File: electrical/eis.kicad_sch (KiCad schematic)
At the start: 26 parts

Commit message: Changed GPS 175 to not have connection to GTS 205x per g3xpert. Moved ELT GPS from GPS 175 and used RS-232 on GDU 460 for GEA 24 backup.
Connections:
- net SERIAL_IN: now reaches GEA24.P241_4 (RS-232_RX)
- net SERIAL_OUT: now reaches GEA24.P241_5 (RS-232_TX)
- net SERIAL_GND: now reaches GEA24.P241_6 (SIGNAL_GND)
- no-connect marks 20 -> 17
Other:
- note removed: "Not enough serial ports on GDU"
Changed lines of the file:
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@@
 	(title_block
 		(title "EIS")
-		(date "2025-09-08")
-		(rev "1.0")
+		(date "2025-09-09")
+		(rev "1.0.1")
 		(company "N78HR")
 	)
@@
 			)
 			(justify left)
-		)
-	)
-	(text "Not enough serial\nports on GDU"
-		(exclude_from_sim no)
-		(at 80.264 39.116 0)
-		(effects
-			(font
-				(size 1.27 1.27)
-			)
 		)
 	)
@@
 	)
 	(no_connect
-		(at 67.31 36.83)
-	)
-	(no_connect
-		(at 67.31 41.91)
-	)
-	(no_connect
 		(at 95.25 134.62)
 	)
@@
 	)
 	(no_connect
-		(at 67.31 39.37)
-	)
-	(no_connect
 		(at 67.31 220.98)
 	)
@@
 	(wire
 		(pts
+			(xy 67.31 41.91) (xy 78.74 41.91)
+		)
+		(stroke
+			(width 0)
+			(type default)
+		)
+	)
+	(wire
+		(pts
 			(xy 86.36 106.68) (xy 67.31 106.68)
 		)
@@
 	(wire
 		(pts
+			(xy 67.31 39.37) (xy 78.74 39.37)
+		)
+		(stroke
+			(width 0)
+			(type default)
+		)
+	)
+	(wire
+		(pts
 			(xy 67.31 177.8) (xy 95.25 177.8)
 		)
@@
 		(pts
 			(xy 67.31 26.67) (xy 78.74 26.67)
+		)
+		(stroke
+			(width 0)
+			(type default)
+		)
+	)
+	(wire
+		(pts
+			(xy 67.31 36.83) (xy 78.74 36.83)
 		)
 		(stroke
@@
 		)
 	)
+	(hierarchical_label "SERIAL_OUT"
+		(shape output)
+		(at 78.74 36.83 0)
+		(effects
+			(font
+				(size 1.27 1.27)
+			)
+			(justify left)
+		)
+	)
 	(hierarchical_label "GEA24_PWR"
 		(shape input)
@@
 		)
 	)
+	(hierarchical_label "SERIAL_GND"
+		(shape passive)
+		(at 78.74 41.91 0)
+		(effects
+			(font
+				(size 1.27 1.27)
+			)
+			(justify left)
+		)
+	)
 	(hierarchical_label "IGN_BAK_LOW_VOLTS"
 		(shape input)
@@
 		(effects
 			(font
+				(size 1.27 1.27)
+			)
+			(justify left)
+		)
+	)
+	(hierarchical_label "SERIAL_IN"
+		(shape input)
+		(at 78.74 39.37 0)
+		(effects
+			(font

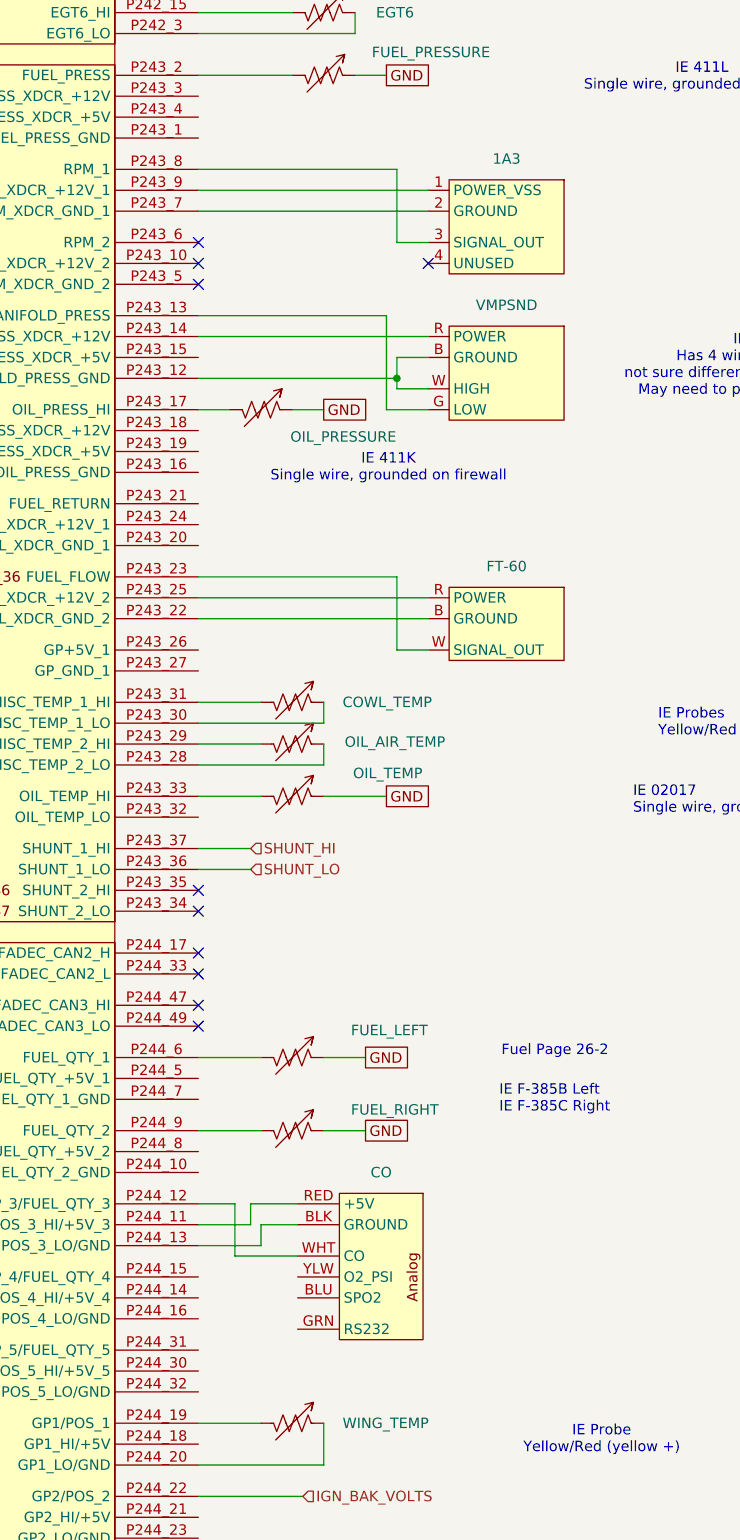
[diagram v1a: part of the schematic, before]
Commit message: Added start, TOGA and Glide lights to cabin power. Changed routing of CAN to match actual.
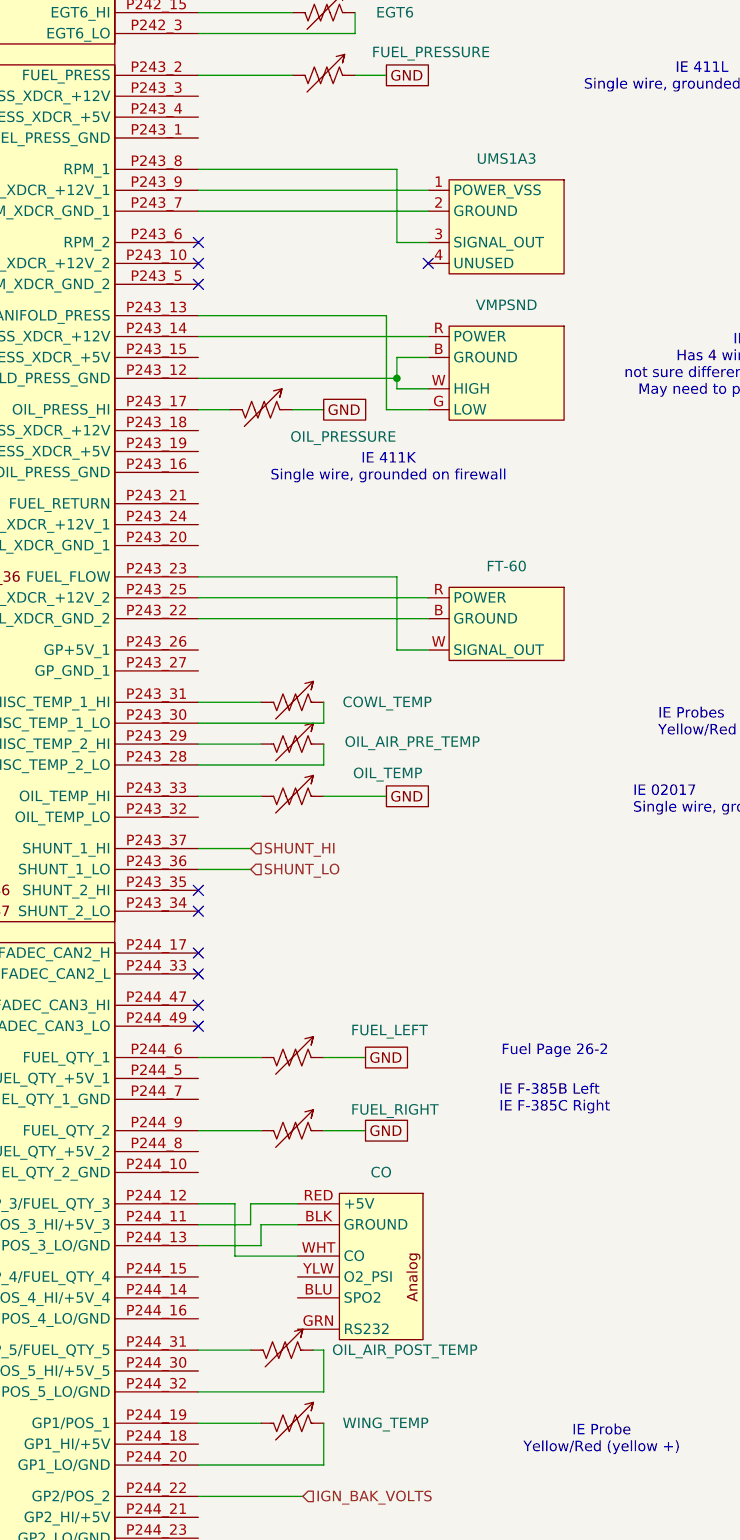
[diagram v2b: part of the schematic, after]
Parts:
- added OIL_AIR_POST_TEMP: R_Variable_US, symbol Device:R_Variable_US
- renumbered OIL_AIR_TEMP to OIL_AIR_PRE_TEMP, 1A3 to UMS1A3
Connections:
- net at GEA24.P244_31 (POS_5/GP_5/FUEL_QTY_5): now also OIL_AIR_POST_TEMP.2
- net at GEA24.P244_32 (POS_5_LO/GND): now also OIL_AIR_POST_TEMP.1
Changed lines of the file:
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@@
 	(title_block
 		(title "EIS")
-		(date "2025-09-09")
-		(rev "1.0.1")
+		(date "2025-09-24")
+		(rev "1.0.4")
 		(company "N78HR")
 	)
@@
 	(wire
 		(pts
+			(xy 67.31 266.7) (xy 73.66 266.7)
+		)
+		(stroke
+			(width 0)
+			(type default)
+		)
+	)
+	(wire
+		(pts
 			(xy 71.755 255.27) (xy 79.375 255.27)
 		)
@@
 	(wire
 		(pts
+			(xy 82.55 266.7) (xy 82.55 271.78)
+		)
+		(stroke
+			(width 0)
+			(type default)
+		)
+	)
+	(wire
+		(pts
 			(xy 67.31 57.15) (xy 78.74 57.15)
 		)
@@
 	(wire
 		(pts
+			(xy 81.28 266.7) (xy 82.55 266.7)
+		)
+		(stroke
+			(width 0)
+			(type default)
+		)
+	)
+	(wire
+		(pts
 			(xy 67.31 111.76) (xy 78.74 111.76)
 		)
@@
 		(pts
 			(xy 67.31 240.03) (xy 74.93 240.03)
+		)
+		(stroke
+			(width 0)
+			(type default)
+		)
+	)
+	(wire
+		(pts
+			(xy 82.55 271.78) (xy 67.31 271.78)
 		)
 		(stroke
@@
 		(on_board yes)
 		(dnp no)
-		(property "Reference" "OIL_AIR_TEMP"
+		(property "Reference" "OIL_AIR_PRE_TEMP"
 			(at 85.09 192.786 90)
 			(effects
@@
 			(project "electrical"
 				(path "/e8ec215a-dbe2-4eba-a577-e50a0a128049/72184f52-5cc1-469a-bd6f-4bd63aea59bf"
-					(reference "OIL_AIR_TEMP")
+					(reference "OIL_AIR_PRE_TEMP")
 					(unit 1)
 				)
@@
 	(symbol
 		(lib_id "Device:R_Variable_US")
+		(at 77.47 266.7 270)
+		(mirror x)
+		(unit 1)
+		(exclude_from_sim no)
+		(in_bom yes)
+		(on_board yes)
+		(dnp no)
+		(property "Reference" "OIL_AIR_POST_TEMP"
+			(at 83.566 266.7 90)
+			(effects
+				(font
+					(size 1.27 1.27)
+				)
+				(justify left)
+			)
+		)
+		(property "Value" "R_Variable_US"
+			(at 76.2382 262.89 0)
+			(effects
+				(font
+					(size 1.27 1.27)
+				)
+				(justify left)
+				(hide yes)
+			)
+		)
+		(property "Footprint" ""
+			(at 77.47 268.478 90)
+			(effects
+				(font
+					(size 1.27 1.27)
+				)
+				(hide yes)
+			)
+		)
+		(property "Datasheet" "~"
+			(at 77.47 266.7 0)
+			(effects
+				(font
+					(size 1.27 1.27)
+				)
+				(hide yes)
+			)
+		)
+		(property "Description" "Variable resistor, US symbol"
+			(at 77.47 266.7 0)
+			(effects
+				(font
+					(size 1.27 1.27)
+				)
+				(hide yes)
+			)
+		)
+		(pin "1"
+		)
+		(pin "2"
+		)
+		(instances
+			(project "electrical"
+				(path "/e8ec215a-dbe2-4eba-a577-e50a0a128049/72184f52-5cc1-469a-bd6f-4bd63aea59bf"
+					(reference "OIL_AIR_POST_TEMP")
+					(unit 1)
+				)
+			)
+		)
+	)
+	(symbol
+		(lib_id "Device:R_Variable_US")
 		(at 82.55 83.82 270)
 		(mirror x)
@@
 		(on_board yes)
 		(dnp no)
-		(property "Reference" "1A3"
+		(property "Reference" "UMS1A3"
 			(at 104.775 121.92 0)
 			(effects
@@
 			(project ""
 				(path "/e8ec215a-dbe2-4eba-a577-e50a0a128049/72184f52-5cc1-469a-bd6f-4bd63aea59bf"
-					(reference "1A3")
+					(reference "UMS1A3")
 					(unit 1)
 				)

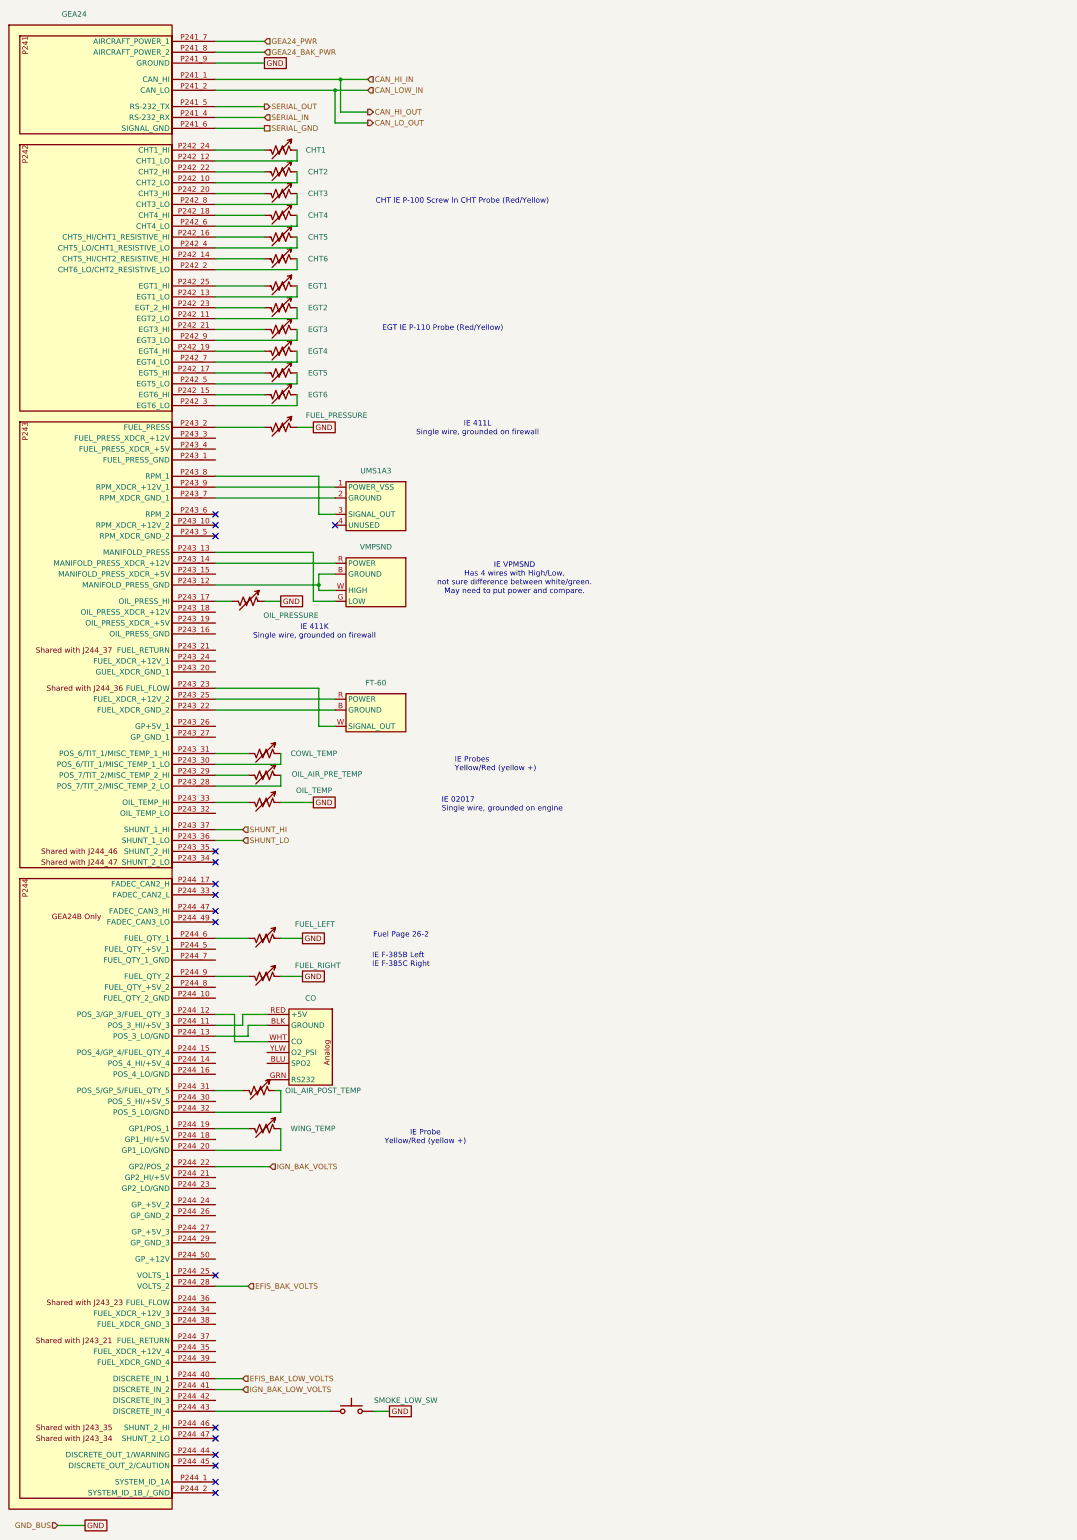
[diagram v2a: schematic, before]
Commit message: Added reuse of US-8A connector for CHT and EGT.
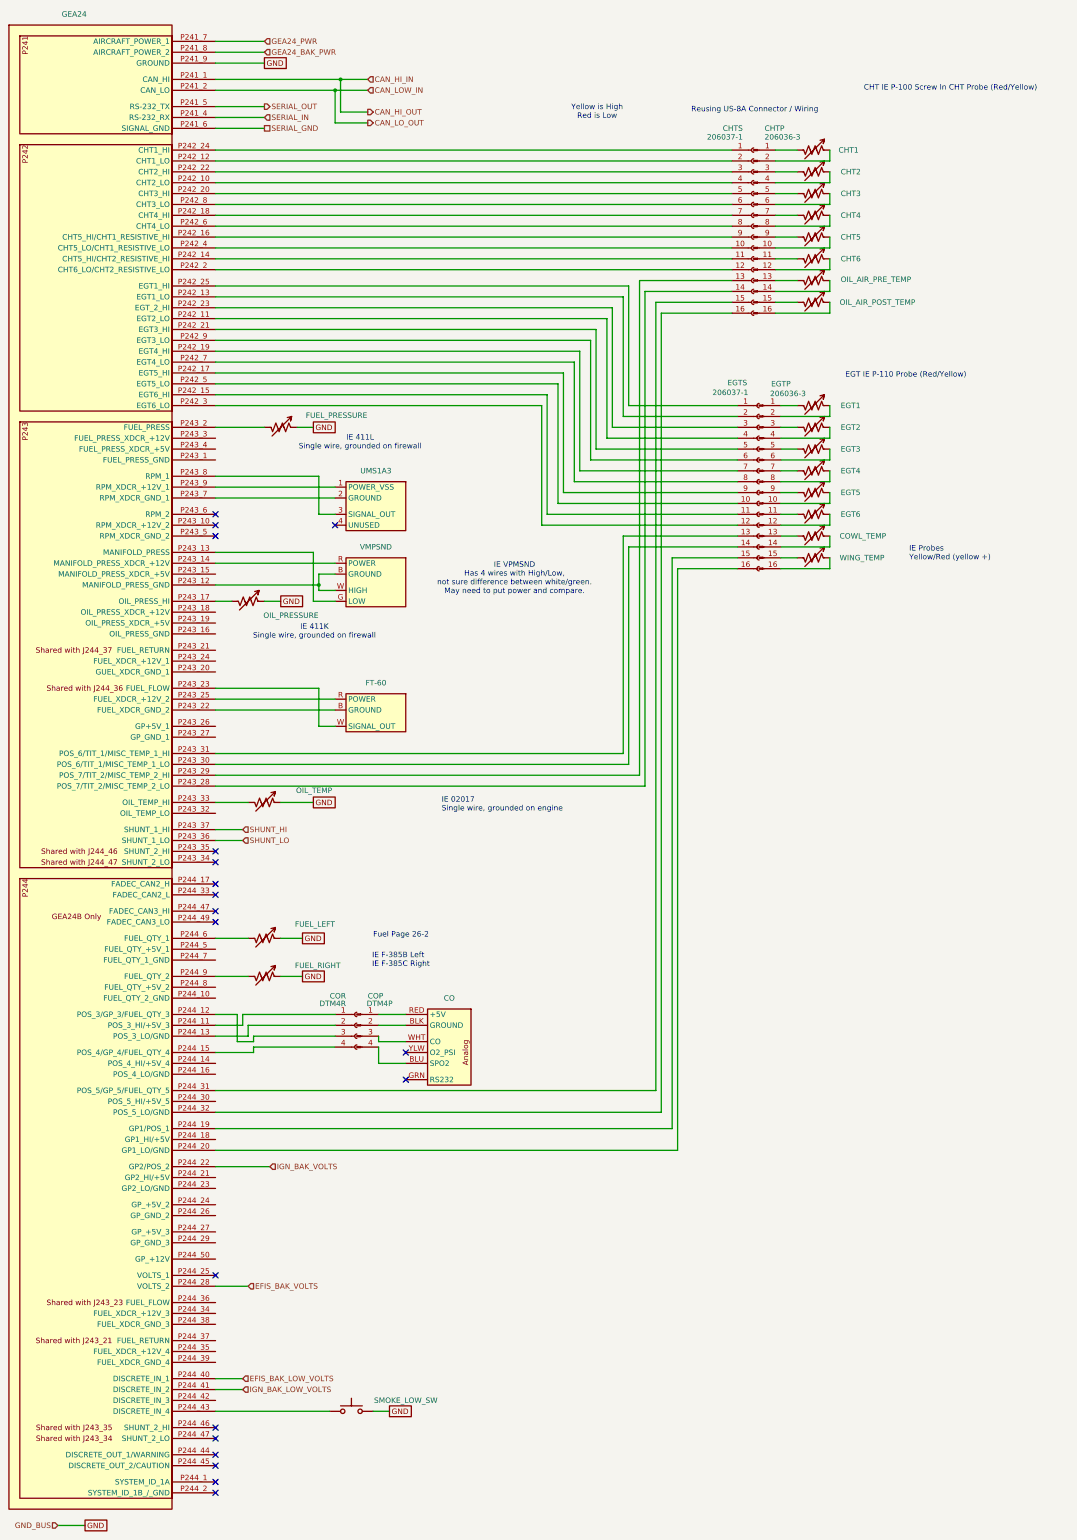
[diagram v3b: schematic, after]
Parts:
- added CHTP, EGTP: 206036-3, symbol Connector:Conn_01x16_Pin
- added CHTS, EGTS: 206037-1, symbol Connector:Conn_01x16_Socket
- added COP: DTM4P, symbol Connector:Conn_01x04_Pin
- added COR: DTM4R, symbol Connector:Conn_01x04_Socket
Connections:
- net at OIL_AIR_PRE_TEMP.1: now also CHTP.14 (Pin_14); no longer GEA24.P243_28 (POS_7/TIT_2/MISC_TEMP_2_LO)
- net at OIL_AIR_PRE_TEMP.2: now also CHTP.13 (Pin_13); no longer GEA24.P243_29 (POS_7/TIT_2/MISC_TEMP_2_HI)
- net at GEA24.P242_6 (CHT4_LO): now also CHTS.8 (Pin_8); no longer CHT4.1
- net at GEA24.P242_18 (CHT4_HI): now also CHTS.7 (Pin_7); no longer CHT4.2
- net at GEA24.P242_2 (CHT6_LO/CHT2_RESISTIVE_LO): now also CHTS.12 (Pin_12); no longer CHT6.1
- net at GEA24.P242_14 (CHT5_HI/CHT2_RESISTIVE_HI): now also CHTS.11 (Pin_11); no longer CHT6.2
- net at GEA24.P242_10 (CHT2_LO): now also CHTS.4 (Pin_4); no longer CHT2.1
- net at GEA24.P242_22 (CHT2_HI): now also CHTS.3 (Pin_3); no longer CHT2.2
- net at GEA24.P242_11 (EGT2_LO): now also EGTS.4 (Pin_4); no longer EGT2.1
- net at GEA24.P242_12 (CHT1_LO): now also CHTS.2 (Pin_2); no longer CHT1.1
- net at GEA24.P242_13 (EGT1_LO): now also EGTS.2 (Pin_2); no longer EGT1.1
- net at GEA24.P242_15 (EGT6_HI): now also EGTS.11 (Pin_11); no longer EGT6.2
- net at GEA24.P242_16 (CHT5_HI/CHT1_RESISTIVE_HI): now also CHTS.9 (Pin_9); no longer CHT5.2
- net at GEA24.P242_17 (EGT5_HI): now also EGTS.9 (Pin_9); no longer EGT5.2
- net at GEA24.P242_19 (EGT4_HI): now also EGTS.7 (Pin_7); no longer EGT4.2
- net at GEA24.P242_20 (CHT3_HI): now also CHTS.5 (Pin_5); no longer CHT3.2
- net at GEA24.P242_21 (EGT3_HI): now also EGTS.5 (Pin_5); no longer EGT3.2
- net at GEA24.P242_23 (EGT_2_HI): now also EGTS.3 (Pin_3); no longer EGT2.2
- net at GEA24.P242_24 (CHT1_HI): now also CHTS.1 (Pin_1); no longer CHT1.2
- net at GEA24.P242_25 (EGT1_HI): now also EGTS.1 (Pin_1); no longer EGT1.2
- net at GEA24.P242_3 (EGT6_LO): now also EGTS.12 (Pin_12); no longer EGT6.1
- net at GEA24.P242_4 (CHT5_LO/CHT1_RESISTIVE_LO): now also CHTS.10 (Pin_10); no longer CHT5.1
- net at GEA24.P242_5 (EGT5_LO): now also EGTS.10 (Pin_10); no longer EGT5.1
- net at GEA24.P242_7 (EGT4_LO): now also EGTS.8 (Pin_8); no longer EGT4.1
- net at GEA24.P242_8 (CHT3_LO): now also CHTS.6 (Pin_6); no longer CHT3.1
- net at GEA24.P242_9 (EGT3_LO): now also EGTS.6 (Pin_6); no longer EGT3.1
- net at GEA24.P243_30 (POS_6/TIT_1/MISC_TEMP_1_LO): now also EGTS.14 (Pin_14); no longer COWL_TEMP.1
- net at GEA24.P243_31 (POS_6/TIT_1/MISC_TEMP_1_HI): now also EGTS.13 (Pin_13); no longer COWL_TEMP.2
- net at CO.RED (+5V): now also COP.1 (Pin_1); no longer GEA24.P244_11 (POS_3_HI/+5V_3)
- net at CO.WHT (CO): now also COP.3 (Pin_3); no longer GEA24.P244_12 (POS_3/GP_3/FUEL_QTY_3)
- net at CO.BLK (GROUND): now also COP.2 (Pin_2); no longer GEA24.P244_13 (POS_3_LO/GND)
- net at GEA24.P244_15 (POS_4/GP_4/FUEL_QTY_4): now also COR.4 (Pin_4)
- net at GEA24.P244_19 (GP1/POS_1): now also EGTS.15 (Pin_15); no longer WING_TEMP.2
- net at GEA24.P244_20 (GP1_LO/GND): now also EGTS.16 (Pin_16); no longer WING_TEMP.1
- net at GEA24.P244_31 (POS_5/GP_5/FUEL_QTY_5): now also CHTS.15 (Pin_15); no longer OIL_AIR_POST_TEMP.2
- net at GEA24.P244_32 (POS_5_LO/GND): now also CHTS.16 (Pin_16); no longer OIL_AIR_POST_TEMP.1
- net at CO.BLU (SPO2): now also COP.4 (Pin_4)
- new net: CHTS.13 (Pin_13), GEA24.P243_29 (POS_7/TIT_2/MISC_TEMP_2_HI)
- new net: CHTS.14 (Pin_14), GEA24.P243_28 (POS_7/TIT_2/MISC_TEMP_2_LO)
- new net: CHT4.1, CHTP.8 (Pin_8)
- new net: CHT4.2, CHTP.7 (Pin_7)
- new net: CHT6.1, CHTP.12 (Pin_12)
- new net: CHT6.2, CHTP.11 (Pin_11)
- new net: CHT2.1, CHTP.4 (Pin_4)
- new net: CHT2.2, CHTP.3 (Pin_3)
- new net: COR.1 (Pin_1), GEA24.P244_11 (POS_3_HI/+5V_3)
- new net: COR.3 (Pin_3), GEA24.P244_12 (POS_3/GP_3/FUEL_QTY_3)
- new net: COR.2 (Pin_2), GEA24.P244_13 (POS_3_LO/GND)
- new net: EGT3.1, EGTP.6 (Pin_6)
- new net: EGT3.2, EGTP.5 (Pin_5)
- new net: CHT1.2, CHTP.1 (Pin_1)
- new net: CHT5.1, CHTP.10 (Pin_10)
- new net: CHTP.15 (Pin_15), OIL_AIR_POST_TEMP.2
- new net: CHTP.16 (Pin_16), OIL_AIR_POST_TEMP.1
- new net: CHT1.1, CHTP.2 (Pin_2)
- new net: CHT3.2, CHTP.5 (Pin_5)
- new net: CHT3.1, CHTP.6 (Pin_6)
- new net: CHT5.2, CHTP.9 (Pin_9)
- new net: EGTP.16 (Pin_16), WING_TEMP.1
- new net: EGTP.15 (Pin_15), WING_TEMP.2
- new net: EGT2.1, EGTP.4 (Pin_4)
- new net: EGT2.2, EGTP.3 (Pin_3)
- new net: EGT1.2, EGTP.1 (Pin_1)
- new net: EGT5.1, EGTP.10 (Pin_10)
- new net: EGT6.2, EGTP.11 (Pin_11)
- new net: EGT6.1, EGTP.12 (Pin_12)
- new net: COWL_TEMP.2, EGTP.13 (Pin_13)
- new net: COWL_TEMP.1, EGTP.14 (Pin_14)
- new net: EGT1.1, EGTP.2 (Pin_2)
- new net: EGT4.2, EGTP.7 (Pin_7)
- new net: EGT4.1, EGTP.8 (Pin_8)
- new net: EGT5.2, EGTP.9 (Pin_9)
- no-connect marks 17 -> 19
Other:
- note added: "Reusing US-8A Connector / Wiring"
- note added: "Yellow is High Red is Low"
- note removed: "IE Probe Yellow/Red (yellow +)"
- moved on the sheet: CHT1, CHT2, CHT3, CHT4, CHT5, CHT6, CO, COWL_TEMP, EGT1, EGT2, EGT3, EGT4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
